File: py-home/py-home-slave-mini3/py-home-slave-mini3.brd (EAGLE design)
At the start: 48.2 x 73.3 mm, 21 parts, among them IC1 uln2308, K1 JS-M1-9V-4, K2 JS-M1-9V-4

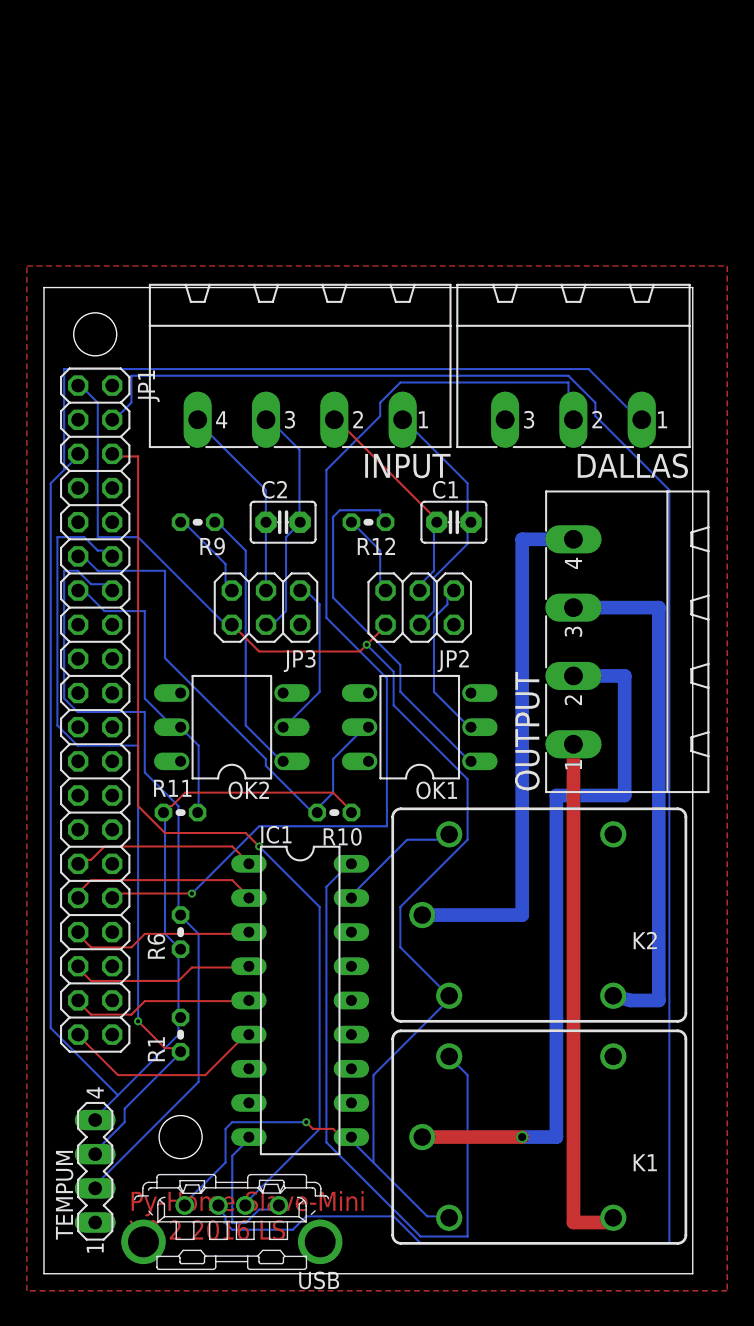
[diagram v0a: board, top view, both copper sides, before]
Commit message: aggiunto py-home-slave a 3 rele per tende e tapparelle
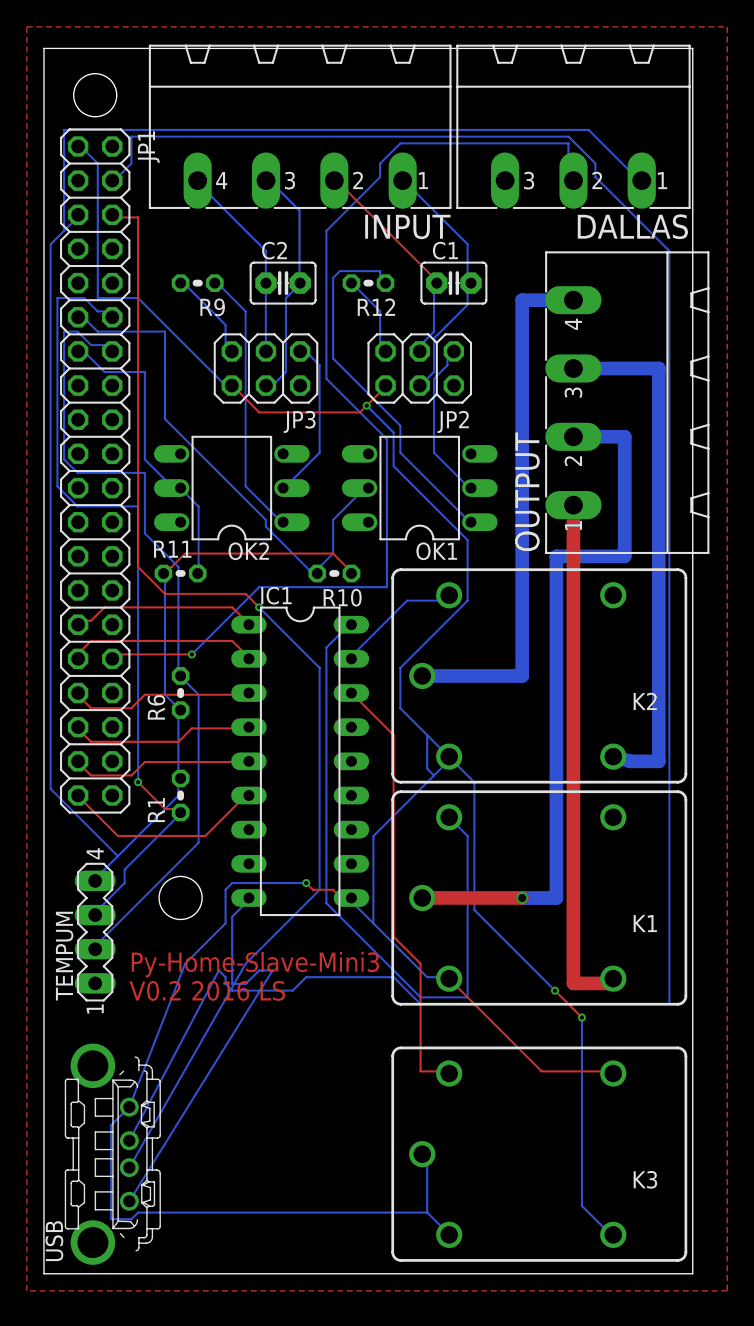
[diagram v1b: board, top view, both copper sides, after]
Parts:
- added K3: JS-M1-9V-4, relay:JS-M
- moved DALLAS 17.8 mm to (39.4, 86.4)
- moved IC1 17.8 mm to (19.1, 38.1)
- moved INPUT 17.8 mm to (19.1, 86.4)
- moved JP1 17.8 mm to (3.81, 59.7)
- moved JP2 17.8 mm to (27.9, 67.3)
- moved JP3 17.8 mm to (16.5, 67.3)
- moved K1 17.8 mm to (36.8, 27.9)
- moved K2 17.8 mm to (36.8, 44.5)
- moved OK1 17.8 mm to (27.9, 58.4)
- moved OK2 17.8 mm to (14.0, 58.4)
- moved R1 17.8 mm to (10.2, 35.6)
- moved R10 17.8 mm to (21.6, 52.1)
- moved R11 17.8 mm to (10.2, 52.1)
- moved R6 17.8 mm to (10.2, 43.2)
- moved TEMPUM 17.8 mm to (3.81, 25.4)
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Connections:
- new net K1: K1.1, K3.NC
- new net K2: K2.1, K3.NO
- net 5V: now also K3.1, K3.C; no longer K1.1, K2.1
- net O3: now also K3.2
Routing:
- net 5V: track 112.3 -> 165.4 mm
- net K2: track 0.00 -> 40.7 mm, vias 0 -> 2
- net O3: track 0.00 -> 32.5 mm
- net GND: track 10.8 -> 30.5 mm
- net USBAD+: track 69.0 -> 86.3 mm
- net K1: track 0.00 -> 15.1 mm
- net USBAD-: track 140.0 -> 154.0 mm
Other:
- board size 48.2 x 73.3 mm -> 48.2 x 91.1 mm
- board text added: "Py-Home-Slave-Mini3 V0.2 2016 LS"
- board text removed: "Py-Home-Slave-Mini V0.2 2016 LS"

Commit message: sistemazione pcb 3 rele
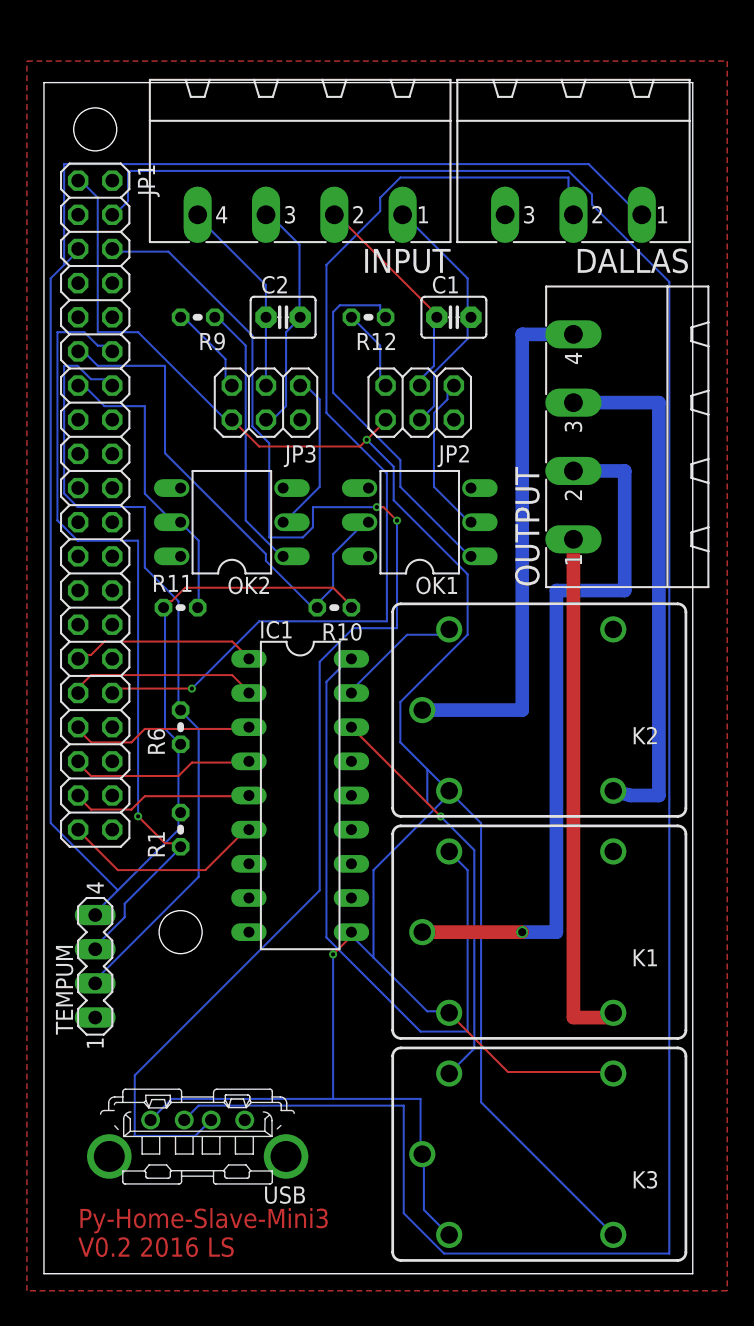
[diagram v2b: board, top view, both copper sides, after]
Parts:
- moved USB 5.68 mm to (11.4, 11.4), turned to 180 degrees
- moved DALLAS 2.54 mm to (39.4, 83.8)
- moved INPUT 2.54 mm to (19.1, 83.8)
- moved JP2 2.54 mm to (27.9, 64.8)
- moved JP3 2.54 mm to (16.5, 64.8)
- moved K2 2.54 mm to (36.8, 41.9)
- moved K1 2.54 mm to (36.8, 25.4)
- moved IC1 2.54 mm to (19.1, 35.6)
- moved JP1 2.54 mm to (3.81, 57.1)
- moved OK1 2.54 mm to (27.9, 55.9)
- moved OK2 2.54 mm to (14.0, 55.9)
- moved OUTPUT 2.54 mm to (44.5, 62.2)
- moved R1 2.54 mm to (10.2, 33.0)
- moved R10 2.54 mm to (21.6, 49.5)
- moved R11 2.54 mm to (10.2, 49.5)
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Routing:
- net GND: track 30.5 -> 0.00 mm
- net 5V: track 165.4 -> 142.6 mm
- net USBAD+: track 86.3 -> 102.2 mm, vias 1 -> 2
- net USBAD-: track 154.0 -> 165.9 mm
- net K2: track 40.7 -> 38.1 mm, vias 2 -> 0
- net O3: track 32.5 -> 30.3 mm, vias 0 -> 1
- net K1: track 15.1 -> 14.1 mm
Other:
- board size 48.2 x 91.1 mm -> 48.2 x 88.6 mm
